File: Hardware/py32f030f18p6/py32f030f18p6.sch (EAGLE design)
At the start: 29 parts, among them IC2 AP2114HA-3.3TRG1, J1 USB_MINI-B_SMT, Y1 DSC6083CI1A-350K000T

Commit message: Remove button replace with header, removed reset pin
Replaced the boot button with a header, removed reset pin
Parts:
- removed J2: (no value), SparkFun-Connectors:CONN_05
- removed R5: (no value), rcl:R-EU_R0805
- removed S3: RESET, SparkFun-Switches:MOMENTARY-SWITCH-SPST-SMD-6.0X3.5MM
- added J7: (no value), SparkFun-Connectors:CONN_04PTH
- JP3: value JUMPER-SMT_2_NC_PASTE_SILK -> 455-1750-1-ND; device SparkFun-Jumpers:JUMPER-SMT_2_NC_PASTE_SILK -> SparkFun-Connectors:CONN_03
- R1, R2: value (none) -> 10K
- U$1: device ch340k-nopad:CH430K -> angelo-ch340k-nopad:CH430K
- renumbered LED to L1, PWR to L2
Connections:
- removed net N$1: JP3.2, R5.2, S3.1
- net +3V3: now also J7.4, JP3.1; no longer J2.5, S3.2
- net GND: now also J7.2, JP3.3; no longer J2.3, R5.1
- net PA13-SWDIO: now also J7.1; no longer J2.2
- net PA14-SWCLK: now also J7.3; no longer J2.4
- net PF2-NRST: no longer J2.1
- net PF4-BOOT0: now also JP3.2; no longer JP3.1

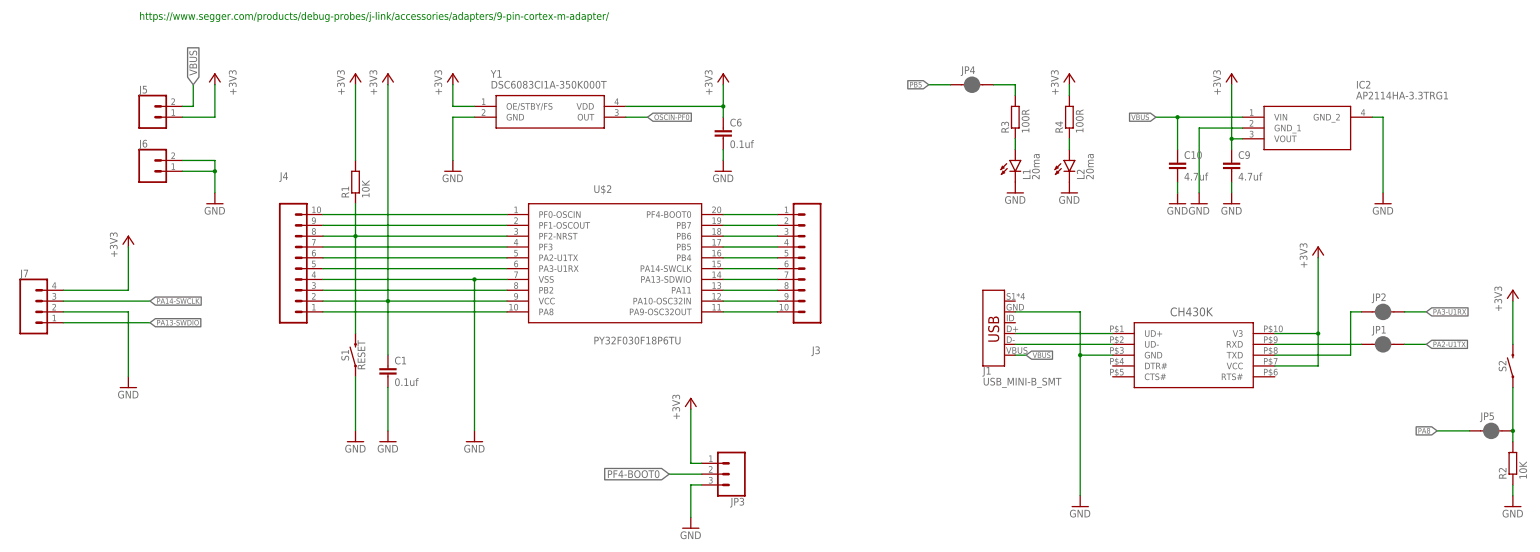
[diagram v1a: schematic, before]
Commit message: Added missing pullup on RX to fix bootloader issue, updated the firmware so it outputs message on uart
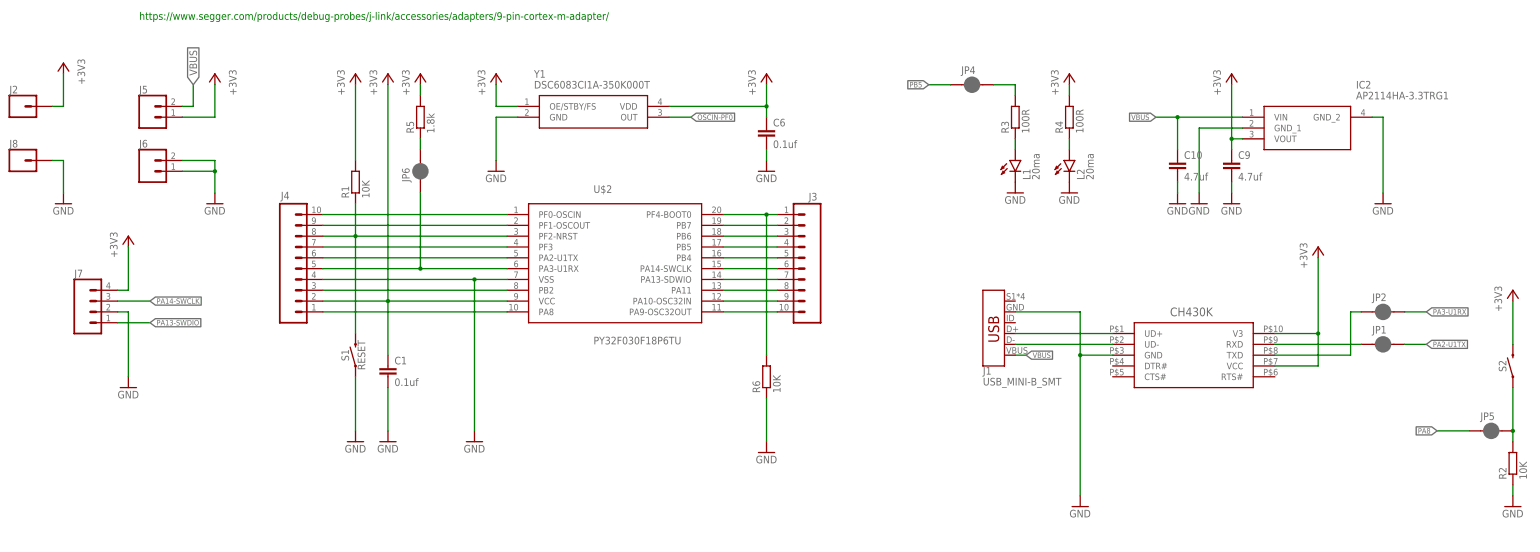
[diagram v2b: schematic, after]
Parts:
- removed JP3: 455-1750-1-ND, SparkFun-Connectors:CONN_03
- added J2, J8: (no value), SparkFun-Connectors:CONN_01
- added JP6: JUMPER-SMT_2_NC_PASTE_SILK, SparkFun-Jumpers:JUMPER-SMT_2_NC_PASTE_SILK
- added R5: 1.8k, rcl:R-EU_R0805
- added R6: 10K, rcl:R-EU_R0805
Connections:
- new net N$1: JP6.2, R5.1
- net +3V3: now also J2.1, R5.2; no longer JP3.1
- net GND: now also J8.1, R6.1; no longer JP3.3
- net PA3-U1RX: now also JP6.1
- net PF4-BOOT0: now also R6.2; no longer JP3.2
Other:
- moved on the sheet: C6, J7, Y1
